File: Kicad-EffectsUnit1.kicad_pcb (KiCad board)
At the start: 2 copper layers, 100 x 100 mm, 121 parts, among them IC101 MCP4725module, IC102 MCP4725module, J101 Doepfer connector, J102 Vin 7-12v, J103 MIDI OUT, J104 Power Conn, J105 CV7 in, J106 Gate1, J107 MIDI IN, J108 CV6 in, J109 Gate2, J110 CV3 in, J111 Gate3, J112 CV1, J113 Gate4, J114 CV2, J115 ControlConn, J116 ControlConn, J117 I2C_Conn, J118 I2C_Conn, Q101 MMBT2222A, Q102 MMBT2222A, SW101 Rotary_Encoder_Switch, U101 TL072, U102 TL072, U103 EL814

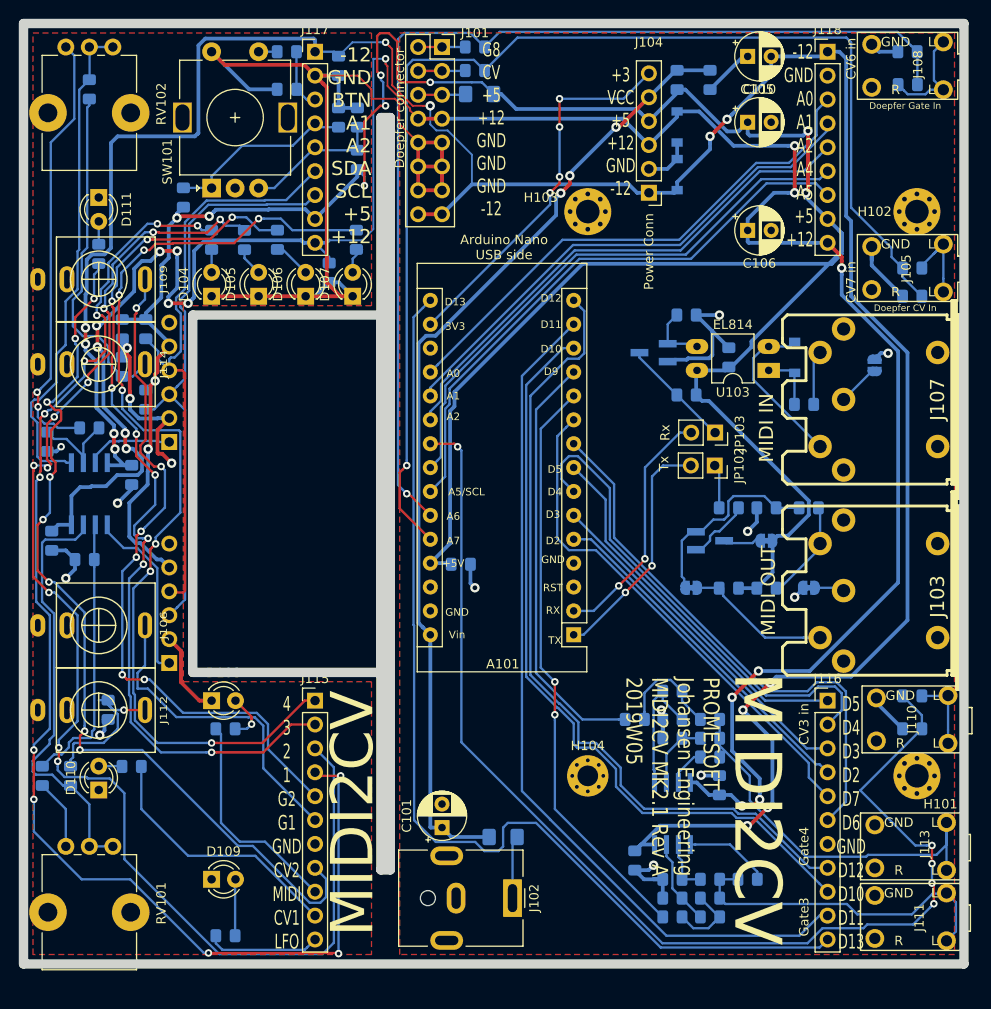
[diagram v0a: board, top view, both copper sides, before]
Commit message: Sch added switches and clipping diodes - init pcb
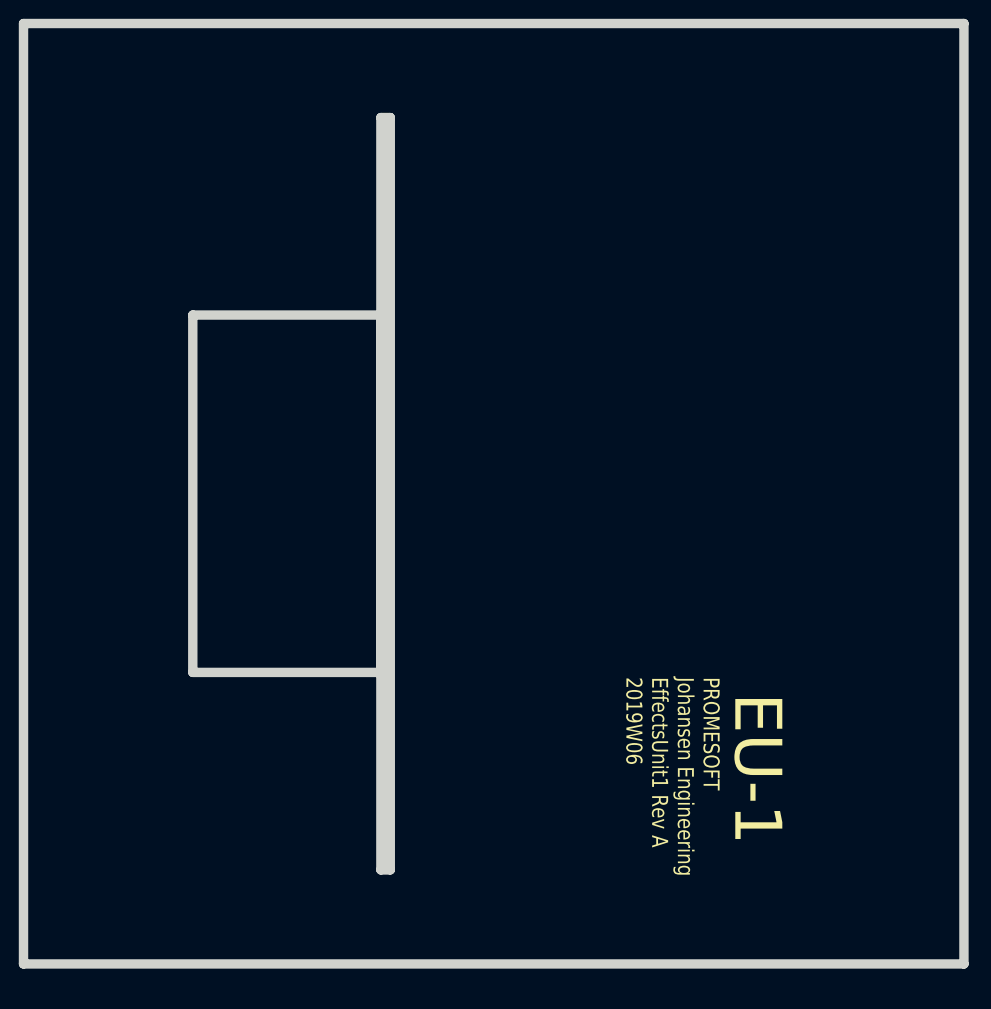
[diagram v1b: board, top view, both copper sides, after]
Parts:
- removed A101: Arduino_Nano_v3.x, Module:Arduino_Nano
- removed C101, C105: 100uF, Capacitor_THT:CP_Radial_D5.0mm_P2.50mm
- removed C102, C103, C104, C107, C108, C109, C111, C112, C113, C116, C122, C123: 100n, Capacitor_SMD:C_0805_2012Metric_Pad1.15x1.40mm_HandSolder
- removed C106, C110: 100uF 16v, Capacitor_THT:CP_Radial_D5.0mm_P2.50mm
- removed C114: 11n, Capacitor_SMD:C_0805_2012Metric_Pad1.15x1.40mm_HandSolder
- removed C115: 22n, Capacitor_SMD:C_0805_2012Metric_Pad1.15x1.40mm_HandSolder
- removed C117, C118: 33n, Capacitor_SMD:C_0805_2012Metric_Pad1.15x1.40mm_HandSolder
- removed C119, C120: 44n, Capacitor_SMD:C_0805_2012Metric_Pad1.15x1.40mm_HandSolder
- removed C121: 47n, Capacitor_SMD:C_0805_2012Metric_Pad1.15x1.40mm_HandSolder
- removed D101, D102: 1N1007, Diode_SMD:D_SOD-123
- removed D103: 1N4148W, Diode_SMD:D_SOD-123
- removed D104: LED1, LED_THT:LED_D3.0mm
- removed D105: LED2, LED_THT:LED_D3.0mm
- removed D106: LED3, LED_THT:LED_D3.0mm
- removed D107: LED4, LED_THT:LED_D3.0mm
- removed D108: LED_MIDI, LED_THT:LED_D3.0mm
- removed D109: LED_LFO, LED_THT:LED_D3.0mm
- removed D110: LED_CV1, LED_THT:LED_D3.0mm
- removed D111: LED_CV2, LED_THT:LED_D3.0mm
- removed F101, F102: Polyfuse, Fuse:Fuse_1206_3216Metric_Pad1.42x1.75mm_HandSolder
- removed H101, H102: 2,5mm, MountingHole:MountingHole_2.5mm_Pad_Via
- removed H103: 2,2mm, MountingHole:MountingHole_2.5mm_Pad_Via
- removed H104: 2,2mm, MountingHole:MountingHole_2.2mm_M2_Pad_Via
- removed IC101, IC102: MCP4725module, Connector_PinSocket_2.54mm:PinSocket_1x06_P2.54mm_Vertical
- removed J101: Doepfer connector, Connector_PinSocket_2.54mm:PinSocket_2x08_P2.54mm_Vertical
- removed J102: Vin 7-12v, Connector_BarrelJack:BarrelJack_CUI_PJ-063AH_Horizontal
- removed J103: MIDI OUT, w_conn_av:din-5
- removed J104: Power Conn, Connector_PinHeader_2.54mm:PinHeader_1x06_P2.54mm_Vertical
- removed J105: CV7 in, Connector_Audio:AudioJack3StereoNarrow-PJ-321
- removed J106: Gate1, AJ-Dropbox-Kicad:PJ301SM
- removed J107: MIDI IN, w_conn_av:din-5
- removed J108: CV6 in, Connector_Audio:AudioJack3StereoNarrow-PJ-321
- removed J109: Gate2, AJ-Dropbox-Kicad:PJ301SM
- removed J110: CV3 in, Connector_Audio:AudioJack3StereoNarrow-PJ-321
- removed J111: Gate3, Connector_Audio:AudioJack3StereoNarrow-PJ-321
- removed J112: CV1, AJ-Dropbox-Kicad:PJ301SM
- removed J113: Gate4, Connector_Audio:AudioJack3StereoNarrow-PJ-321
- removed J114: CV2, AJ-Dropbox-Kicad:PJ301SM
- removed J115, J116: ControlConn, Connector_PinHeader_2.54mm:PinHeader_1x11_P2.54mm_Vertical
- removed J117, J118: I2C_Conn, Connector_PinHeader_2.54mm:PinHeader_1x09_P2.54mm_Vertical
- removed JP101: GND MIDI OUT, Jumper:SolderJumper-2_P1.3mm_Bridged_RoundedPad1.0x1.5mm
- removed JP102: Tx, Connector_PinSocket_2.54mm:PinSocket_1x02_P2.54mm_Vertical
- removed JP103: Rx, Connector_PinSocket_2.54mm:PinSocket_1x02_P2.54mm_Vertical
- removed JP104: GND MIDI IN, Jumper:SolderJumper-2_P1.3mm_Open_RoundedPad1.0x1.5mm
- removed Q101, Q102: MMBT2222A, Package_TO_SOT_SMD:SOT-23_Handsoldering
- removed R101, R102, R119, R126: 1k, Resistor_SMD:R_0805_2012Metric_Pad1.15x1.40mm_HandSolder
- removed R103: 10M, Resistor_SMD:R_0805_2012Metric_Pad1.15x1.40mm_HandSolder
- removed R104, R105: 11k, Resistor_SMD:R_0805_2012Metric_Pad1.15x1.40mm_HandSolder
- removed R106, R107: 8k2, Resistor_SMD:R_0805_2012Metric_Pad1.15x1.40mm_HandSolder
- removed R108: 110R, Resistor_SMD:R_0805_2012Metric_Pad1.15x1.40mm_HandSolder
- removed R109, R112: OPEN, Resistor_SMD:R_0805_2012Metric_Pad1.15x1.40mm_HandSolder
- removed R110, R118, R121: 220R, Resistor_SMD:R_0805_2012Metric_Pad1.15x1.40mm_HandSolder
- removed R111, R115: 0R, Jumper:SolderJumper-2_P1.3mm_Bridged_RoundedPad1.0x1.5mm
- removed R113, R114: 22k, Resistor_SMD:R_0805_2012Metric_Pad1.15x1.40mm_HandSolder
- removed R116: 2k, Resistor_SMD:R_0805_2012Metric_Pad1.15x1.40mm_HandSolder
- removed R117, R132, R133, R134, R137, R140, R141, R142, R143: 680R, Resistor_SMD:R_0805_2012Metric_Pad1.15x1.40mm_HandSolder
- removed R120, R122, R125, R127, R130, R131, R144, R145, R146: 10k, Resistor_SMD:R_0805_2012Metric_Pad1.15x1.40mm_HandSolder
- removed R123, R124, R128, R129: 33k, Resistor_SMD:R_0805_2012Metric_Pad1.15x1.40mm_HandSolder
- removed R135, R136, R138, R139: 44k, Resistor_SMD:R_0805_2012Metric_Pad1.15x1.40mm_HandSolder
- removed R147: 133R, Resistor_SMD:R_0805_2012Metric_Pad1.15x1.40mm_HandSolder
- removed R148: 144R, Resistor_SMD:R_0805_2012Metric_Pad1.15x1.40mm_HandSolder
- removed RV101, RV102: 10k, Potentiometer_THT:Potentiometer_Alps_RK09K_Single_Vertical
- removed SW101: Rotary_Encoder_Switch, Rotary_Encoder:RotaryEncoder_Alps_EC11E-Switch_Vertical_H20mm
- removed U101, U102: TL072, AJ-Dropbox-Kicad:AJ_SO-8_5.3x6.2mm_P1.27mm
- removed U103: EL814, Package_DIP:DIP-4_W7.62mm_LongPads
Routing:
- net +5V: track 288.6 -> 0.00 mm, vias 10 -> 0
- net -12V: track 273.8 -> 0.00 mm, vias 12 -> 0
- net +12V: track 258.7 -> 0.00 mm, vias 16 -> 0
- net GND: track 216.6 -> 0.00 mm, vias 15 -> 0
- net LED-CV2: track 182.1 -> 0.00 mm, vias 8 -> 0
- net LED2: track 179.9 -> 0.00 mm, vias 10 -> 0
- net LED1: track 176.8 -> 0.00 mm, vias 11 -> 0
- net LED3: track 147.7 -> 0.00 mm, vias 9 -> 0
- net LED4: track 145.1 -> 0.00 mm, vias 7 -> 0
- net A7: track 131.8 -> 0.00 mm, vias 1 -> 0
- net Gate2: track 128.3 -> 0.00 mm, vias 6 -> 0
- net A3: track 125.5 -> 0.00 mm, vias 5 -> 0
- net SDA: track 123.8 -> 0.00 mm
- net SCL: track 123.6 -> 0.00 mm
- net LED_LFO: track 121.7 -> 0.00 mm
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- removed copper zone on F.Cu, net GND
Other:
- board text added: "EU-1"
- board text added: "PROMESOFT Johansen Engineering EffectsUnit1 Rev A 2019W06"
- board text removed: "+3 VCC +5 +12 GND -12"
- board text removed: "+5V"
- board text removed: "-12 GND A0 A1 A2 A4 A5 +5 +12"
- board text removed: "-12 GND BTN A1 A2 SDA SCL +5 +12"
- board text removed: "3V3"
- board text removed: "4 3 2 1 G2 G1 GND CV2 MIDI CV1 LFO"
- board text removed: "A0"
- board text removed: "A1"
- board text removed: "A2"
- board text removed: "A5/SCL"
- board text removed: "A6"
- board text removed: "A7"
- board text removed: "Arduino Nano USB side"
- board text removed: "D10"
- board text removed: "D11"
- board text removed: "D12"
- board text removed: "D13"
- board text removed: "D2"
- board text removed: "D3"
- board text removed: "D4"
- board text removed: "D5"
- board text removed: "D5 D4 D3 D2 D7 D6 GND D12 D10 D11 D13"
- board text removed: "D9"
- board text removed: "Doepfer CV In"
- board text removed: "Doepfer Gate In"
- board text removed: "G8 CV +5 +12 GND GND GND -12"
- board text removed: "GND"
- board text removed: "MIDI2CV"
- board text removed: "PROMESOFT Johansen Engineering MIDI2CV MK2.1 Rev A 2019W05"
- board text removed: "PROMESOFT Johansen Enginerring SubSection - 2019W05 DAC Gate CV MK2.1RevA"
- board text removed: "RST"
- board text removed: "RX"
- board text removed: "TX"
- board text removed: "Tip + Shield GND"
- board text removed: "Vin"
- board text removed: "Vin to +5V JP"
